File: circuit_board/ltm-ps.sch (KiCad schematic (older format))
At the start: 2 parts, among them P1 CONN_01X02, U1 LTM4609

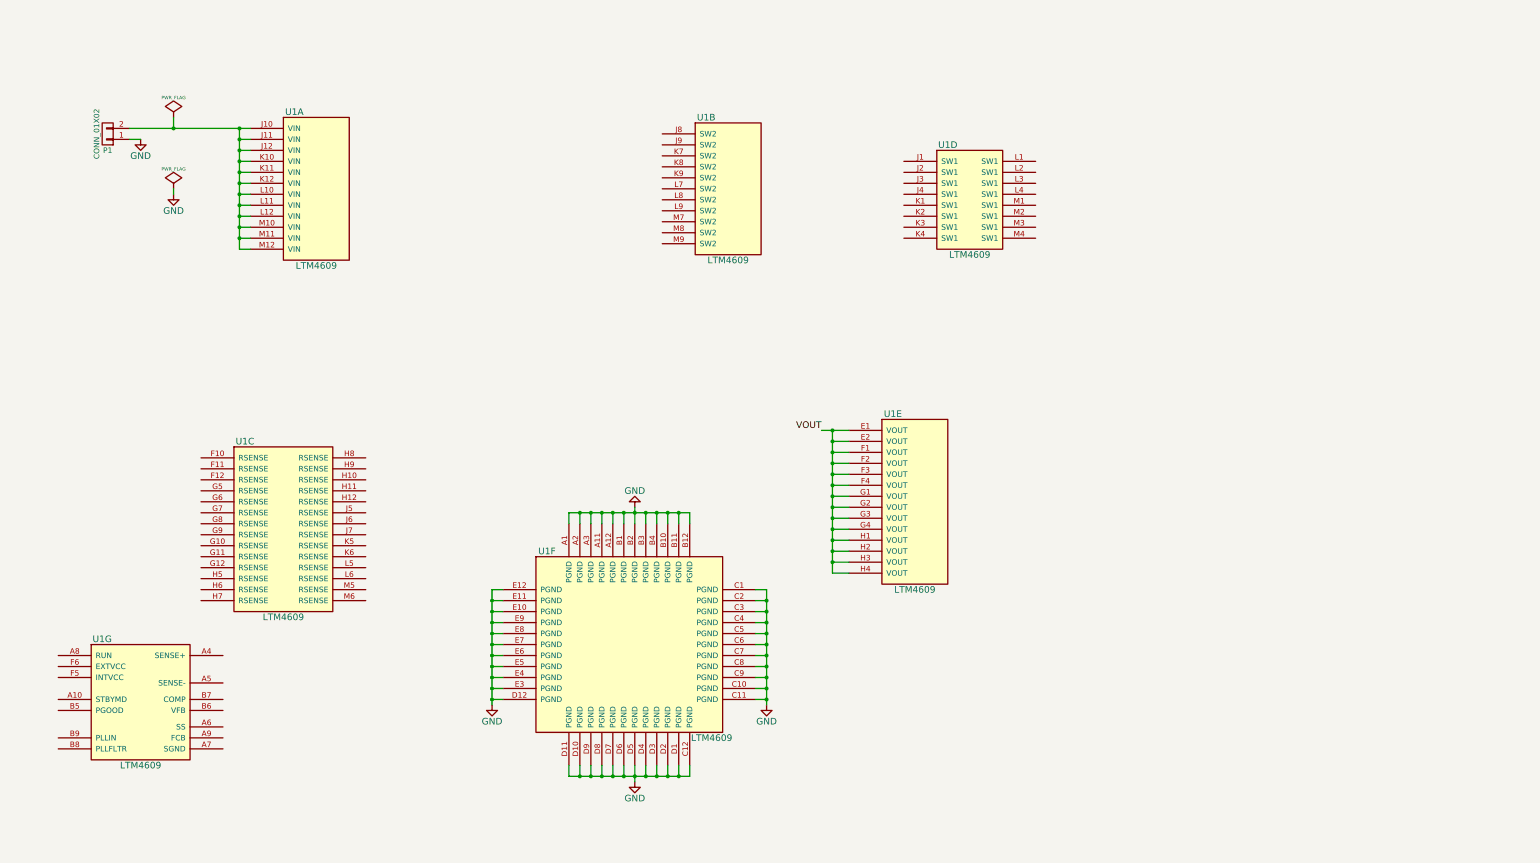
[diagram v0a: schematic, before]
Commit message: restart schamatic based on PoE feature with LTM8050 step-down converter
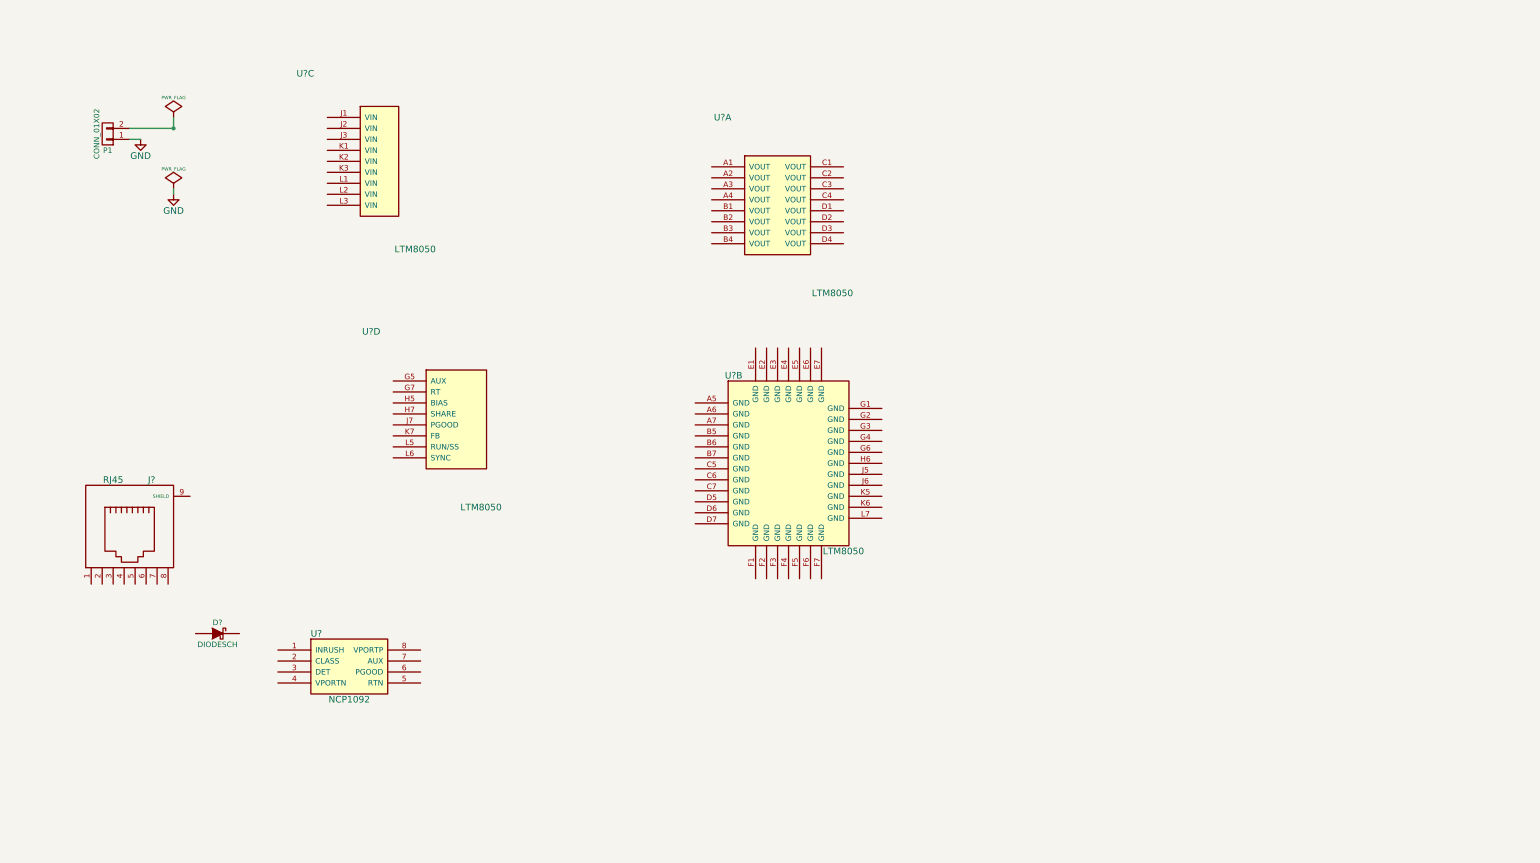
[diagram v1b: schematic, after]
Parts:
- removed U1: LTM4609, symbol LTM4609
- added D?: DIODESCH, symbol DIODESCH
- added J?: RJ45, symbol RJ45
- added U? (x4): LTM8050, symbol LTM8050
- added U?: NCP1092, symbol NCP1092

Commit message: add main IC in library and schematics
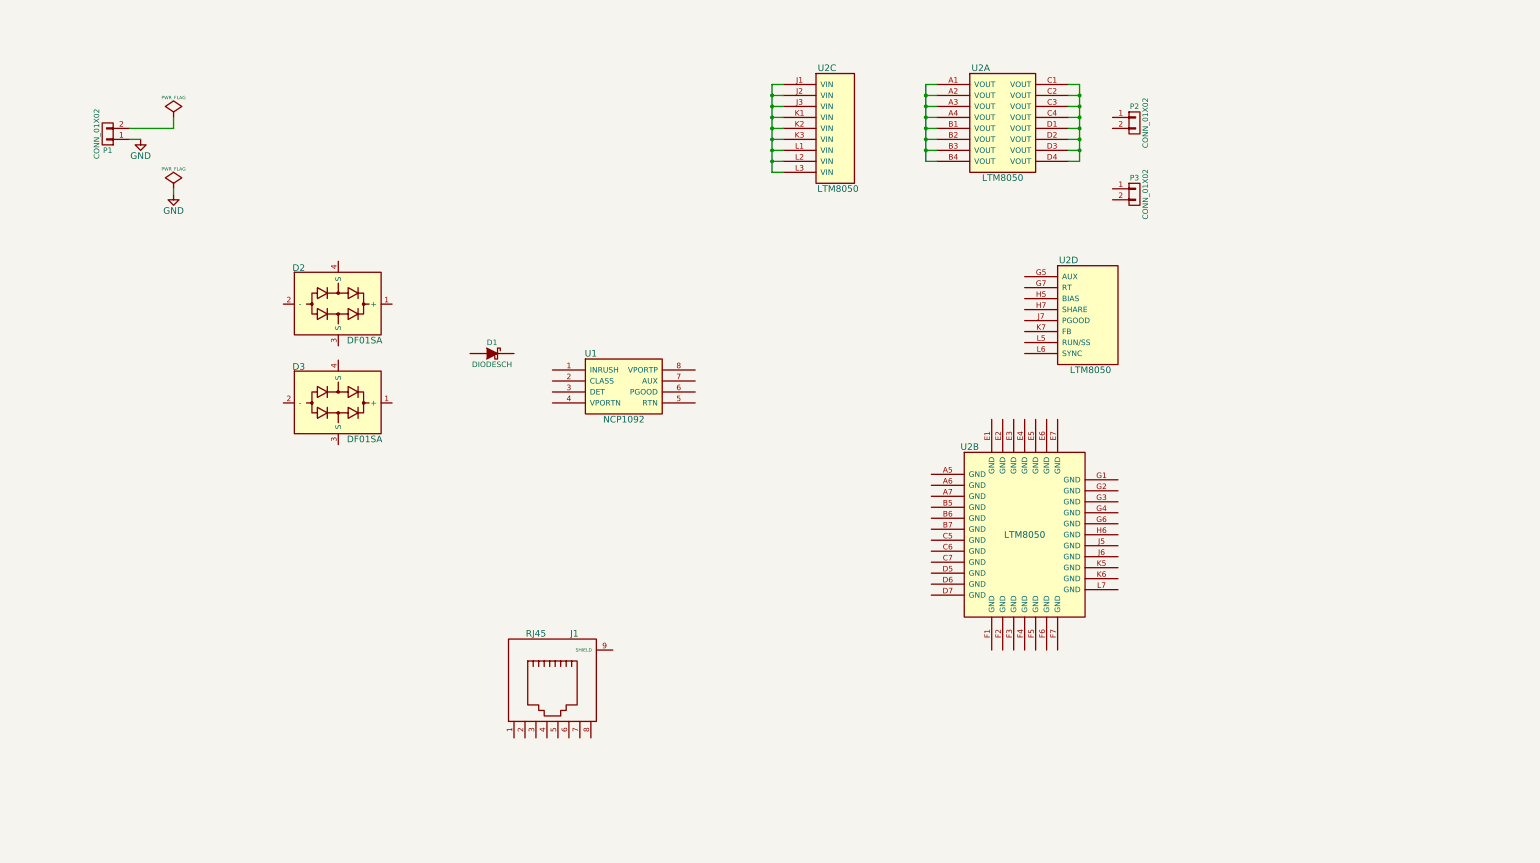
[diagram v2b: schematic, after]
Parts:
- added D2, D3: DF01SA, symbol DF01SA
- added P2, P3: CONN_01X02, symbol CONN_01X02
- gave numbers to parts that had none: 4
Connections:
- net at U2.A1 (VOUT): now also U2.A2 (VOUT), U2.A3 (VOUT), U2.A4 (VOUT), U2.B1 (VOUT), U2.B2 (VOUT), U2.B3 (VOUT), U2.B4 (VOUT)
- net at U2.C1 (VOUT): now also U2.C2 (VOUT), U2.C3 (VOUT), U2.C4 (VOUT), U2.D1 (VOUT), U2.D2 (VOUT), U2.D3 (VOUT), U2.D4 (VOUT)
- net at U2.J1 (VIN): now also U2.J2 (VIN), U2.J3 (VIN), U2.K1 (VIN), U2.K2 (VIN), U2.K3 (VIN), U2.L1 (VIN), U2.L2 (VIN), U2.L3 (VIN)
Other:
- moved on the sheet: D1, J1, U1, U2A, U2B, U2C, U2D
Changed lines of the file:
@@
-EESchema Schematic File Version 2  date Thu 29 Jan 2015 12:16:26 AM CET
+EESchema Schematic File Version 2  date Thu 29 Jan 2015 06:25:49 PM CET
 LIBS:power
 LIBS:device
@@
 LIBS:valves
 LIBS:onsemi
+LIBS:ltm-ps-cache
 EELAYER 25  0
 EELAYER END
@@
 Sheet 1 1
 Title ""
-Date "28 jan 2015"
+Date "29 jan 2015"
 Rev ""
 Comp ""
@@
 Comment4 ""
 $EndDescr
-$Comp
-L DIODESCH D?
+Wire Wire Line
+	1700 1350 1800 1350
+Connection ~ 7550 950
+Wire Wire Line
+	7650 950  7550 950
+Connection ~ 7550 1150
+Wire Wire Line
+	7650 1150 7550 1150
+Connection ~ 7550 1350
+Wire Wire Line
+	7650 1350 7550 1350
+Connection ~ 7550 1550
+Wire Wire Line
+	7650 1550 7550 1550
+Connection ~ 10350 950
+Wire Wire Line
+	10250 950  10350 950
+Connection ~ 10350 1150
+Wire Wire Line
+	10250 1150 10350 1150
+Connection ~ 10350 1350
+Wire Wire Line
+	10250 1350 10350 1350
+Wire Wire Line
+	10250 1550 10350 1550
+Wire Wire Line
+	10350 1550 10350 850
+Wire Wire Line
+	10350 850  10250 850
+Connection ~ 8950 1050
+Wire Wire Line
+	9050 1050 8950 1050
+Connection ~ 8950 1250
+Wire Wire Line
+	9050 1250 8950 1250
+Connection ~ 8950 1450
+Wire Wire Line
+	9050 1450 8950 1450
+Wire Wire Line
+	2100 1800 2100 1850
+Wire Wire Line
+	9050 850  8950 850
+Wire Wire Line
+	8950 850  8950 1550
+Wire Wire Line
+	8950 1550 9050 1550
+Wire Wire Line
+	8950 1350 9050 1350
+Connection ~ 8950 1350
+Wire Wire Line
+	8950 1150 9050 1150
+Connection ~ 8950 1150
+Wire Wire Line
+	8950 950  9050 950
+Connection ~ 8950 950
+Wire Wire Line
+	10350 1450 10250 1450
+Connection ~ 10350 1450
+Wire Wire Line
+	10350 1250 10250 1250
+Connection ~ 10350 1250
+Wire Wire Line
+	10350 1050 10250 1050
+Connection ~ 10350 1050
+Wire Wire Line
+	7650 850  7550 850
+Wire Wire Line
+	7550 850  7550 1650
+Wire Wire Line
+	7550 1650 7650 1650
+Wire Wire Line
+	7550 1450 7650 1450
+Connection ~ 7550 1450
+Wire Wire Line
+	7550 1250 7650 1250
+Connection ~ 7550 1250
+Wire Wire Line
+	7550 1050 7650 1050
+Connection ~ 7550 1050
+Wire Wire Line
+	1700 1250 2100 1250
+Wire Wire Line
+	2100 1250 2100 1150
+$Comp
+L CONN_01X02 P3
+U 1 1 54CA5C28
+P 10850 1850
+F 0 "P3" H 10850 2000 50  0000 C CNN
+F 1 "CONN_01X02" V 10950 1850 50  0000 C CNN
+	1    10850 1850
+	1    0    0    -1
+$EndComp
+$Comp
+L CONN_01X02 P2
+U 1 1 54CA5C1E
+P 10850 1200
+F 0 "P2" H 10850 1350 50  0000 C CNN
+F 1 "CONN_01X02" V 10950 1200 50  0000 C CNN
+	1    10850 1200
+	1    0    0    -1
+$EndComp
+$Comp
+L DF01SA D3
+U 1 1 54CA5BE8
+P 3600 3750
+F 0 "D3" H 3240 4080 60  0000 C CNN
+F 1 "DF01SA" H 3840 3420 60  0000 C CNN
+	1    3600 3750
+	1    0    0    -1
+$EndComp
+$Comp
+L DF01SA D2
+U 1 1 54CA5BE6
+P 3600 2850
+F 0 "D2" H 3240 3180 60  0000 C CNN
+F 1 "DF01SA" H 3840 2520 60  0000 C CNN
+	1    3600 2850
+	1    0    0    -1
+$EndComp
+$Comp
+L DIODESCH D1
 U 1 1 54C96D83
-P 2500 5850
-F 0 "D?" H 2500 5950 50  0000 C CNN
-F 1 "DIODESCH" H 2500 5750 50  0000 C CNN
-	1    2500 5850
-	1    0    0    -1
-$EndComp
-$Comp
-L RJ45 J?
+P 5000 3300
+F 0 "D1" H 5000 3400 50  0000 C CNN
+F 1 "DIODESCH" H 5000 3200 50  0000 C CNN
+	1    5000 3300
+	1    0    0    -1
+$EndComp
+$Comp
+L RJ45 J1
 U 1 1 54C96745
-P 1700 4950
-F 0 "J?" H 1900 5450 60  0000 C CNN
-F 1 "RJ45" H 1550 5450 60  0000 C CNN
-	1    1700 4950
-	1    0    0    -1
-$EndComp
-$Comp
-L NCP1092 U?
+P 5550 6350
+F 0 "J1" H 5750 6850 60  0000 C CNN
+F 1 "RJ45" H 5400 6850 60  0000 C CNN
+	1    5550 6350
+	1    0    0    -1
+$EndComp
+$Comp
+L NCP1092 U1
 U 1 1 54C966D1
-P 3700 6150
-F 0 "U?" H 3400 6450 60  0000 C CNN
-F 1 "NCP1092" H 3700 5850 60  0000 C CNN
-	1    3700 6150
-	1    0    0    -1
-$EndComp
-$Comp
-L LTM8050 U?
+P 6200 3600
+F 0 "U1" H 5900 3900 60  0000 C CNN
+F 1 "NCP1092" H 6200 3300 60  0000 C CNN
+	1    6200 3600
+	1    0    0    -1
+$EndComp
+$Comp
+L LTM8050 U2
 U 4 1 54C96627
-P 4400 3900
-F 0 "U?" H 3900 4700 60  0000 C CNN
-F 1 "LTM8050" H 4900 3100 60  0000 C CNN
-	4    4400 3900
-	1    0    0    -1
-$EndComp
-$Comp
-L LTM8050 U?
+P 10150 2950
+F 0 "U2" H 10250 3450 60  0000 C CNN
+F 1 "LTM8050" H 10450 2450 60  0000 C CNN
+	4    10150 2950
+	1    0    0    -1
+$EndComp
+$Comp
+L LTM8050 U2
 U 3 1 54C9661E
-P 3800 1550
-F 0 "U?" H 3300 2350 60  0000 C CNN
-F 1 "LTM8050" H 4300 750 60  0000 C CNN
-	3    3800 1550
-	1    0    0    -1
-$EndComp
-$Comp
-L LTM8050 U?
+P 7950 1250
+F 0 "U2" H 8050 1800 60  0000 C CNN
+F 1 "LTM8050" H 8150 700 60  0000 C CNN
+	3    7950 1250
+	1    0    0    -1
+$EndComp
+$Comp
+L LTM8050 U2
 U 2 1 54C96618
-P 7700 4300
-F 0 "U?" H 7200 5100 60  0000 C CNN
-F 1 "LTM8050" H 8200 3500 60  0000 C CNN
-	2    7700 4300
-	1    0    0    -1
-$EndComp
-$Comp
-L LTM8050 U?
+P 9850 4950
+F 0 "U2" H 9350 5750 60  0000 C CNN
+F 1 "LTM8050" H 9850 4950 60  0000 C CNN
+	2    9850 4950
+	1    0    0    -1
+$EndComp
+$Comp
+L LTM8050 U2
 U 1 1 54C9660D
-P 7600 1950
-F 0 "U?" H 7100 2750 60  0000 C CNN
-F 1 "LTM8050" H 8100 1150 60  0000 C CNN
-	1    7600 1950
-	1    0    0    -1
-$EndComp
-Wire Wire Line
-	1700 1250 2100 1250
-Wire Wire Line
-	2100 1800 2100 1850
-Wire Wire Line
-	1700 1350 1800 1350
-Wire Wire Line
-	2100 1250 2100 1150
-Connection ~ 2100 1250
-$Comp
-L GND #PWR?
+P 9650 1200
+F 0 "U2" H 9450 1700 60  0000 C CNN
+F 1 "LTM8050" H 9650 700 60  0000 C CNN
+	1    9650 1200
+	1    0    0    -1
+$EndComp
+$Comp
+L GND #PWR2
 U 1 1 54C01912
 P 2100 1850
-F 0 "#PWR?" H 2100 1600 60  0001 C CNN
+F 0 "#PWR2" H 2100 1600 60  0001 C CNN
 F 1 "GND" H 2100 1700 60  0000 C CNN
 	1    2100 1850
@@
 $EndComp
 $Comp
-L PWR_FLAG #FLG?
+L PWR_FLAG #FLG2
 U 1 1 54C0190D
 P 2100 1800
-F 0 "#FLG?" H 2100 1895 30  0001 C CNN
+F 0 "#FLG2" H 2100 1895 30  0001 C CNN
 F 1 "PWR_FLAG" H 2100 1980 30  0000 C CNN
 	1    2100 1800
@@
 $EndComp
 $Comp
-L PWR_FLAG #FLG?
+L PWR_FLAG #FLG1
 U 1 1 54C01907
 P 2100 1150
-F 0 "#FLG?" H 2100 1245 30  0001 C CNN
+F 0 "#FLG1" H 2100 1245 30  0001 C CNN
 F 1 "PWR_FLAG" H 2100 1330 30  0000 C CNN
 	1    2100 1150
@@
 $EndComp
 $Comp
-L GND #PWR?
+L GND #PWR1
 U 1 1 54C018EC
 P 1800 1350
-F 0 "#PWR?" H 1800 1100 60  0001 C CNN
+F 0 "#PWR1" H 1800 1100 60  0001 C CNN
 F 1 "GND" H 1800 1200 60  0000 C CNN
 	1    1800 1350

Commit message: add LTM800 and NCP1092 ICs settings components. Miss RJ45 with magnetics connector
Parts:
- removed D2, D3: DF01SA, symbol DF01SA
- added C1: 4.7u, symbol C
- added C2: 100u, symbol C
- added D2, D3: DF01S, symbol DIODE_RECTIFIER
- added D4: TVS, symbol TVS
- added JP1: JUMPER3, symbol JUMPER3
- added R1: 93.1k, symbol R
- added R2: 89.4k, symbol R
- added R3: 24.9k, symbol R
- added R4: 4.42k, symbol R
- added R5: 178k, symbol R
- added R6: 150k, symbol R
- added R7: 100k, symbol R
- D1: value DIODESCH -> S5BC-13-F
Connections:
- net labels added: PoE_PGOOD, VAUX, VPORT_N, VPORT_P
- wire segments 32 -> 109
- no-connect marks 0 -> 2
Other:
- moved on the sheet: U2B

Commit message: tie ltm8050 sync pin to ground and refactor ncp1092 to diode rectifiers cabling
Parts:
- removed J1: RJ45, symbol RJ45
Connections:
- net labels added: +5V, AUX
- wire segments 109 -> 130
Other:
- moved on the sheet: D1, P1, U1, U2C

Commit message: add schematic comments and wire jumper
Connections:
- net labels removed: PoE_PGOOD
- wire segments 130 -> 132
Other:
- note added: "Auxiliary source input - 7.5V to 58V"
- note added: "For the prototype version, this jumper allows to select\nwhich signal will enable the DC/DC converter.\n- NCP1092 PGOOD\n- VIN (VPORT_P/VAUX)"
- note added: "R1 sets LTM8050 switching frequency to 400kHz\nR2 sets LTM8050 output voltage to 5.2V"
- moved on the sheet: P2, P3, U2A, U2B, U2D

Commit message: check ERC rules
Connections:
- net labels added: vout_5V@2A
- net labels removed: +5V
- wire segments 132 -> 134
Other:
- note added: "For the prototype version, this jumper allows to select\nwhich signal will enable the DC/DC converter.\n- NCP1092 PGOOD\n- VIN (VPORT_P/Auxiliary source)"
- note removed: "For the prototype version, this jumper allows to select\nwhich signal will enable the DC/DC converter.\n- NCP1092 PGOOD\n- VIN (VPORT_P/VAUX)"
- moved on the sheet: P2, P3, U2A, U2B
